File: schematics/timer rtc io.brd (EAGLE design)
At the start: 180 x 120 mm, 78 parts, among them T1 BC547, U1 74HC245, U10 74HC688, U11 74HC30, U12 74HC00, U13 74HC32, U14 74HC04, U15 74HC08, U16 74HC688, U17 74HC138, U19 74HC573, U2 74HC245, U20 74HC573, U21 74HC573, U22 74HC573, U23 74HC573, U24 NE555, U3 74HC245, U4 74HC688, U5 Z84C30, U6 74HC74, U7 74HC590, U8 74HC688, U9 BQ4845, X1 32.768KHz, Y1 4.096MHz

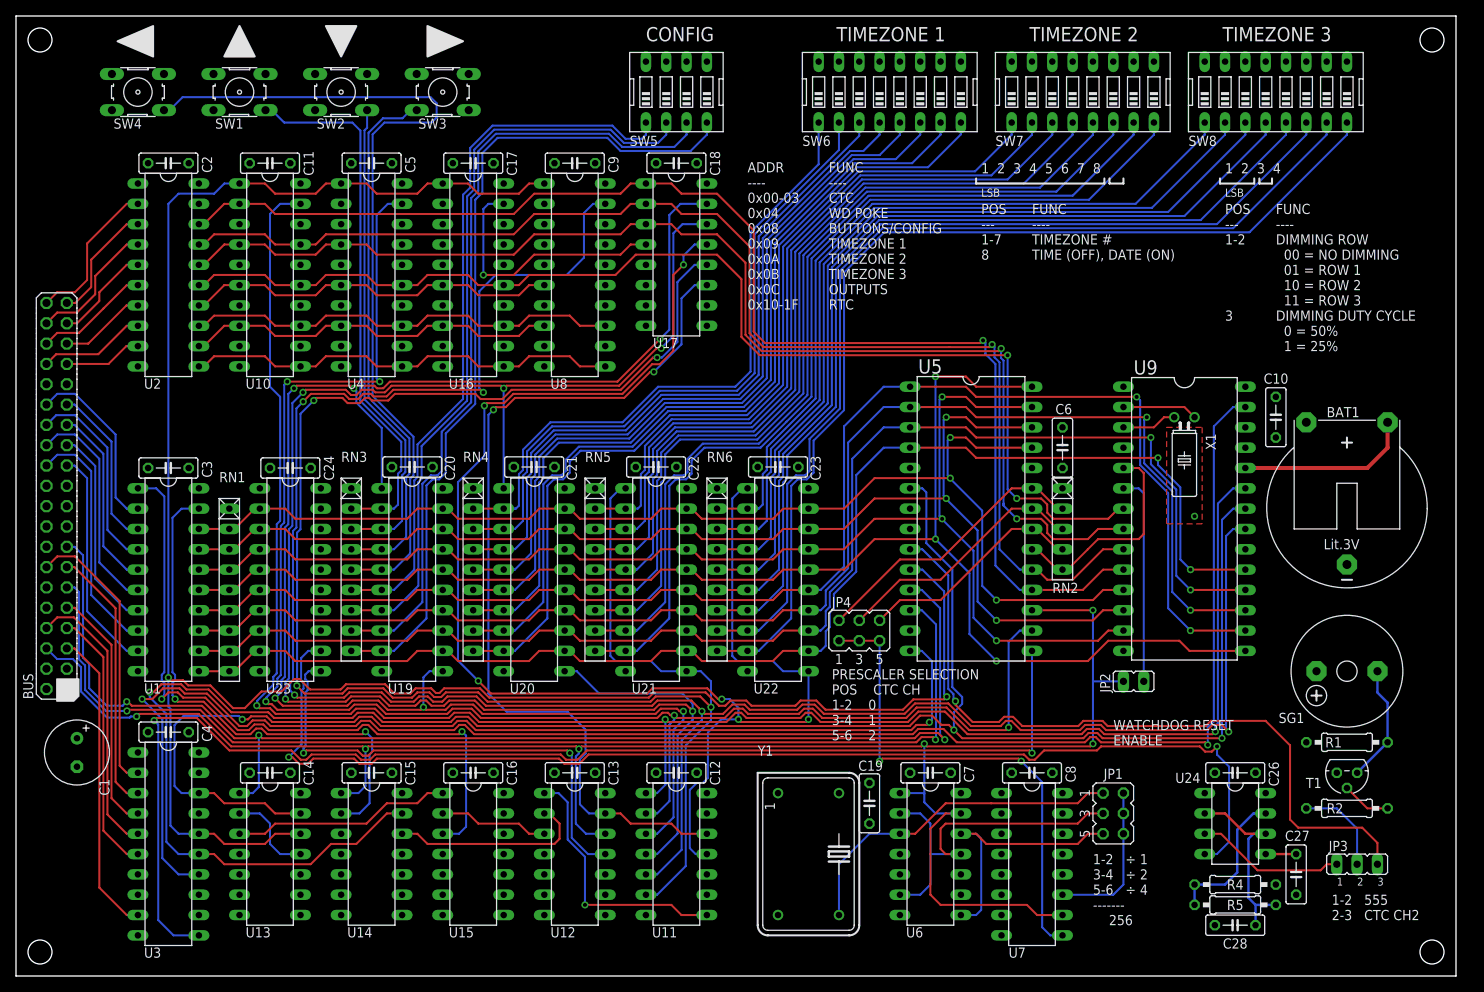
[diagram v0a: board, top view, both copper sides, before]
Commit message: Finalise PCB layout for timer/rtc/io board
Moved the CTC and RTC chips to the unbuffed side of the data bus, and modified direction and enable logic for data bus buffer
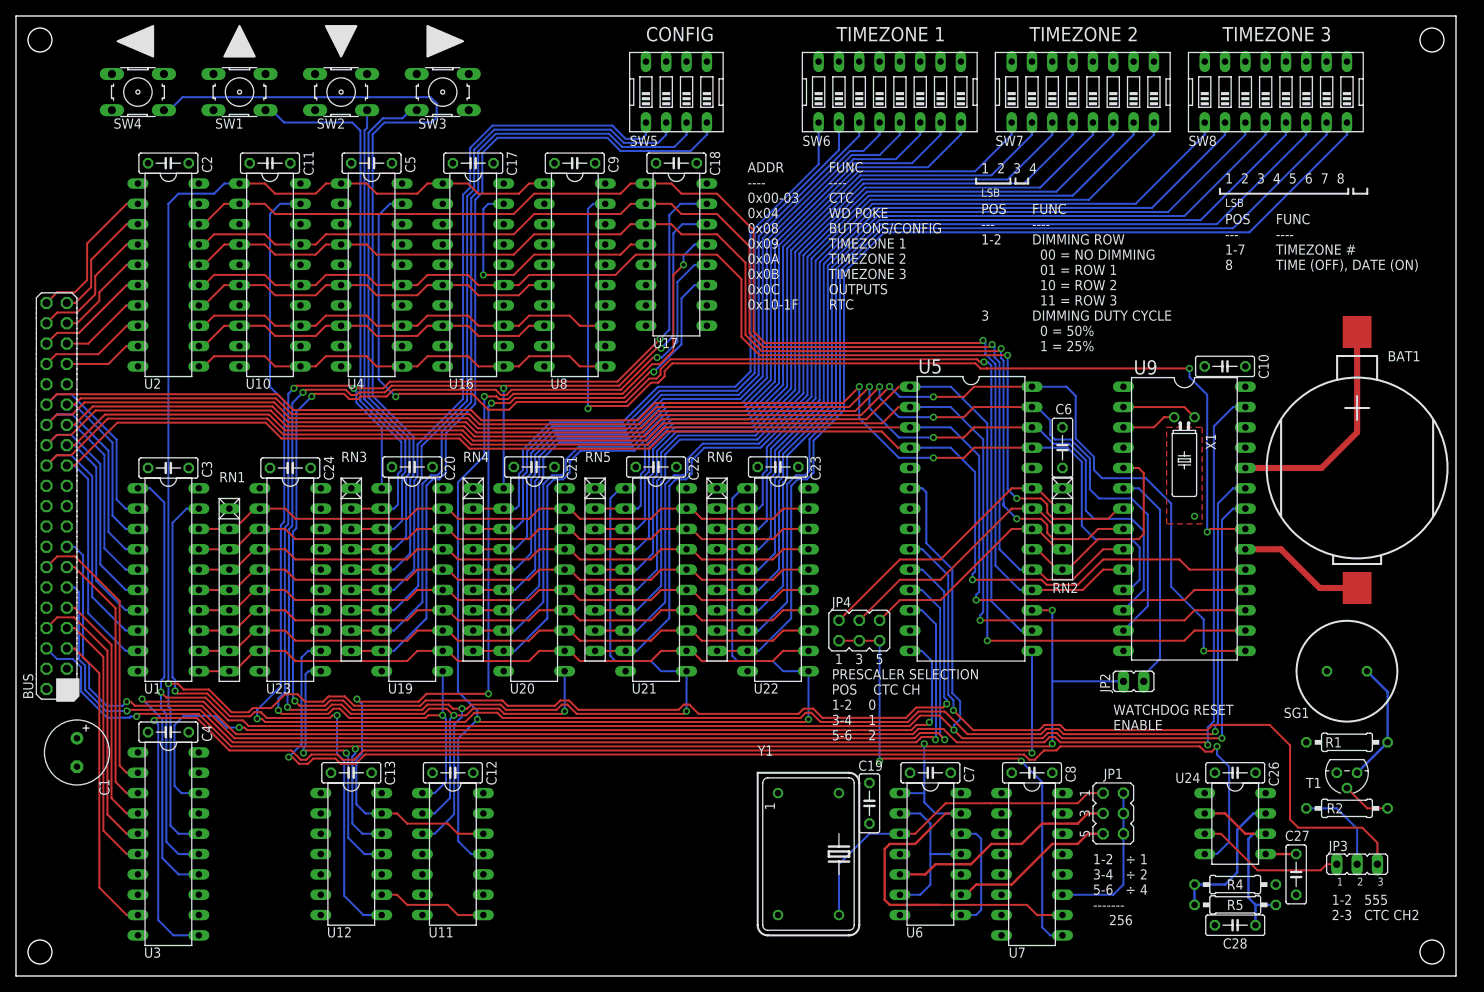
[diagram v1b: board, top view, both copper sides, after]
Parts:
- removed C14, C15, C16: 100nF, rcl:C050-025X075
- removed U13: 74HC32, 74xx-us:DIL14
- removed U14: 74HC04, 74xx-us:DIL14
- removed U15: 74HC08, 74xx-us:DIL14
- BAT1: device battery:CR2032H -> Z80 clock:CR2032-SMD
- SG1: value (none) -> PKM13EPYH4000X; device buzzer:F/CM12P -> Z80 clock:PKM13EPYH400X
- moved C12 27.9 mm to (54.6, 25.4)
- moved C13 27.9 mm to (41.9, 25.4)
- moved U11 27.9 mm to (54.6, 15.2)
- moved U12 27.9 mm to (41.9, 15.2)
- moved C10 8.98 mm to (151.1, 76.2), turned to 180 degrees
- moved BAT1 5.24 mm to (167.6, 63.5), turned to 270 degrees
- turned SG1 to 0 degrees
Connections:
- removed net DIR: U1.1, U15.3
- removed net N$48: U13.3, U15.1
- removed net N$49: BUS.23, U1.9
- removed net N$51: U12.2, U14.12
- removed net N$65: BUS.24, U1.8
- removed net N$66: BUS.25, U1.7
- removed net N$67: BUS.26, U1.6
- removed net N$68: BUS.27, U1.5
- removed net N$69: BUS.28, U1.4
- removed net N$70: BUS.29, U1.3
- removed net N$71: BUS.30, U1.2
- removed net N$87: U12.3, U15.2
- removed net N$91: U13.11, U13.2
- new net !OBD!: U1.19, U12.8
- new net D0`: BUS.30, U1.2, U5.25, U9.11
- new net D1`: BUS.29, U1.3, U5.26, U9.12
- new net D2`: BUS.28, U1.4, U5.27, U9.13
- new net D3`: BUS.27, U1.5, U5.28, U9.15
- new net D4`: BUS.26, U1.6, U5.1, U9.16
- new net D5`: BUS.25, U1.7, U5.2, U9.17
- new net D6`: BUS.24, U1.8, U5.3, U9.18
- new net D7`: BUS.23, U1.9, U5.4, U9.19
- new net N$64: U4.19, U5.16
- net !IEO!: no longer U13.1
- net !IORQ!: no longer U13.12
- net !M1!: no longer U13.13
- net !RD!: now also U1.1; no longer U14.13
- net !RESET!: no longer U14.1
- net +5V: now also SG1.1, U11.4, U11.5, U11.6, U12.10; no longer C14.1, C15.1, C16.1, SG1.+, U13.14, U14.14, U15.14
- net D0: no longer U5.25, U9.11
- net D1: no longer U5.26, U9.12
- net D2: no longer U5.27, U9.13
- net D3: no longer U5.28, U9.15
- net D4: no longer U5.1, U9.16
- net D5: no longer U5.2, U9.17
- net D6: no longer U5.3, U9.18
- net D7: no longer U5.4, U9.19
- net GND: now also U12.1, U12.2; no longer C14.2, C15.2, C16.2, U12.10, U12.9, U13.10, U13.4, U13.5, U13.7, U13.9, U14.11, U14.3, U14.5, U14.7, U14.9, U15.10, U15.12, U15.13, U15.4, U15.5, U15.7, U15.9
- net N$1: no longer JP1.3
- net N$3: no longer U11.1
- net N$36: now also JP1.5, U6.9; no longer U11.8, U12.1
- net N$45: now also U11.1; no longer U11.3
- net N$46: now also U11.2; no longer U11.4
- net N$5: now also U11.8, U12.9; no longer U11.5, U8.19, U9.21
- net N$58: no longer JP1.5
- net N$60: now also SG1.2; no longer SG1.-
- net N$7: now also U8.19, U9.21; no longer U11.2, U4.19, U5.16
- net N$9: now also JP1.3, U6.5; no longer U1.19, U14.2
- net N$90: now also U11.3; no longer U11.6
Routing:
- net N$5: track 274.6 -> 13.8 mm, vias 5 -> 0
- net D4`: track 0.00 -> 212.5 mm, vias 0 -> 1
- net D6`: track 0.00 -> 205.0 mm, vias 0 -> 1
- net D5`: track 0.00 -> 203.1 mm, vias 0 -> 1
- net D3`: track 0.00 -> 202.5 mm, vias 0 -> 3
- net D7`: track 0.00 -> 198.2 mm, vias 0 -> 1
- net D2`: track 0.00 -> 194.8 mm, vias 0 -> 2
- net D0`: track 0.00 -> 185.5 mm, vias 0 -> 2
- net D1`: track 0.00 -> 183.7 mm, vias 0 -> 2
- net N$64: track 0.00 -> 141.9 mm, vias 0 -> 2
- net D3: track 182.9 -> 81.5 mm, vias 3 -> 0
- net D4: track 182.7 -> 81.5 mm, vias 2 -> 0
- net D5: track 178.6 -> 81.5 mm, vias 2 -> 0
- net D6: track 173.5 -> 81.5 mm, vias 2 -> 0
- net D7: track 169.0 -> 81.5 mm, vias 2 -> 0
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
